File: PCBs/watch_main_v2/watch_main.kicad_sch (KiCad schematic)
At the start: 1 part, among them U101 Watch_Outline_V2

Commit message: Schematic v2 complete
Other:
- added sheet STM32 Power (stm32_power.kicad_sch)
- sheet Bluetooth ports: added SWD; removed none
- sheet Display Connector ports: added AVDD, ELVDD, ELVSS, SWIRE, TP_I2C, TP_INT, TP_RST; removed +4V6, -2V2, OLED_EN
- sheet Display Power ports: added AVDD, AVDDEN, ELVDD, ELVSS, SWIRE; removed none
- sheet Expansion Connector ports: added GPIO1, GPIO2, NRF_SWD, STM32_SWD, UART, USB; removed none
- sheet STM32 ports: added AVDDEN, GPIO1, GPIO2, I2C2, I2C6, SPI1, SWD, SWIRE, TP_INT, TP_RST, USART1, USART6, USB; removed USART2
- sheet Sensors ports: added SPI; removed none
- note added: "Power"
- note removed: "RF Circuits"
- moved on the sheet: U101

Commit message: 190 Unrouted traces
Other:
- sheet Bluetooth ports: added none; removed SWD
- sheet Expansion Connector ports: added none; removed NRF_SWD, STM32_SWD
- sheet Micro SD ports: added EN; removed none
- sheet STM32 ports: added none; removed SWD
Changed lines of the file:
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@@
+    (stroke (width 0) (type default))
+  )
+  (wire (pts (xy 165.1 76.2) (xy 231.14 76.2))
     (stroke (width 0) (type default))
   )
@@
     (stroke (width 0) (type default))
   )
-  (bus (pts (xy 165.1 88.9) (xy 231.14 88.9))
+  (bus (pts (xy 165.1 91.44) (xy 231.14 91.44))
     (stroke (width 0) (type default))
   )
@@
     (stroke (width 0) (type default))
   )
-  (bus (pts (xy 63.5 81.28) (xy 73.66 81.28))
-    (stroke (width 0) (type default))
-  )
   (wire (pts (xy 165.1 33.02) (xy 185.42 33.02))
     (stroke (width 0) (type default))
@@
     (stroke (width 0) (type default))
   )
-  (bus (pts (xy 63.5 78.74) (xy 129.54 78.74))
-    (stroke (width 0) (type default))
-  )
   (wire (pts (xy 63.5 25.4) (xy 129.54 25.4))
     (stroke (width 0) (type default))
@@
     (stroke (width 0) (type default))
   )
-  (bus (pts (xy 73.66 88.9) (xy 73.66 81.28))
-    (stroke (width 0) (type default))
-  )
   (bus (pts (xy 88.9 134.62) (xy 88.9 147.32))
     (stroke (width 0) (type default))
@@
     (stroke (width 0) (type default))
   )
-  (wire (pts (xy 165.1 91.44) (xy 231.14 91.44))
+  (wire (pts (xy 165.1 93.98) (xy 231.14 93.98))
     (stroke (width 0) (type default))
   )
@@
     (stroke (width 0) (type default))
   )
-  (wire (pts (xy 165.1 93.98) (xy 231.14 93.98))
+  (wire (pts (xy 165.1 96.52) (xy 231.14 96.52))
     (stroke (width 0) (type default))
   )
@@
   )
   (wire (pts (xy 63.5 129.54) (xy 83.82 129.54))
-    (stroke (width 0) (type default))
-  )
-  (bus (pts (xy 83.82 88.9) (xy 73.66 88.9))
     (stroke (width 0) (type default))
   )
@@
     (effects (font (size 1.27 1.27)) (justify left bottom))
   )
-  (label "STM32_SWD{SWD}" (at 88.9 78.74 0) (fields_autoplaced)
-    (effects (font (size 1.27 1.27)) (justify left bottom))
-  )
   (label "SPI1{SPI}" (at 170.18 109.22 0) (fields_autoplaced)
     (effects (font (size 1.27 1.27)) (justify left bottom))
   )
-  (label "NRF_SWD{SWD}" (at 66.04 81.28 0) (fields_autoplaced)
-    (effects (font (size 1.27 1.27)) (justify left bottom))
-  )
   (label "LPUART1{UART}" (at 111.76 88.9 0) (fields_autoplaced)
     (effects (font (size 1.27 1.27)) (justify left bottom))
@@
     (effects (font (size 1.27 1.27)) (justify left bottom))
   )
-  (label "I2C1{I2C}" (at 193.04 88.9 0) (fields_autoplaced)
+  (label "I2C1{I2C}" (at 193.04 91.44 0) (fields_autoplaced)
     (effects (font (size 1.27 1.27)) (justify left bottom))
   )
@@
       (effects (font (size 1.27 1.27)) (justify left top))
     )
-    (pin "STM32_SWD" bidirectional (at 63.5 78.74 0)
-      (effects (font (size 1.27 1.27)) (justify right))
-    )
-    (pin "NRF_SWD" bidirectional (at 63.5 81.28 0)
-      (effects (font (size 1.27 1.27)) (justify right))
-    )
     (pin "USB" bidirectional (at 63.5 71.12 0)
       (effects (font (size 1.27 1.27)) (justify right))
@@
     )
   )
-  (sheet (at 231.14 86.36) (size 25.4 10.16) (fields_autoplaced)
+  (sheet (at 231.14 88.9) (size 25.4 10.16) (fields_autoplaced)
     (stroke (width 0.3048) (type solid) (color 108 142 191 1))
     (fill (color 218 232 252 1.0000))
-    (property "Sheetname" "Touch Connector" (at 231.14 85.5722 0)
-      (effects (font (size 1.27 1.27)) (justify left bottom))
-    )
-    (property "Sheetfile" "touch_connector.kicad_sch" (at 231.14 97.1808 0)
-      (effects (font (size 1.27 1.27)) (justify left top))
-    )
-    (pin "I2C" bidirectional (at 231.14 88.9 180)
-      (effects (font (size 1.27 1.27)) (justify left))
-    )
-    (pin "IRQN" output (at 231.14 91.44 180)
-      (effects (font (size 1.27 1.27)) (justify left))
-    )
-    (pin "RST" input (at 231.14 93.98 180)
+    (property "Sheetname" "Touch Connector" (at 231.14 88.1122 0)
+      (effects (font (size 1.27 1.27)) (justify left bottom))
+    )
+    (property "Sheetfile" "touch_connector.kicad_sch" (at 231.14 99.7208 0)
+      (effects (font (size 1.27 1.27)) (justify left top))
+    )
+    (pin "I2C" bidirectional (at 231.14 91.44 180)
+      (effects (font (size 1.27 1.27)) (justify left))
+    )
+    (pin "IRQN" output (at 231.14 93.98 180)
+      (effects (font (size 1.27 1.27)) (justify left))
+    )
+    (pin "RST" input (at 231.14 96.52 180)
       (effects (font (size 1.27 1.27)) (justify left))
     )
@@
       (effects (font (size 1.27 1.27)) (justify right))
     )
-    (pin "SWD" bidirectional (at 83.82 88.9 180)
-      (effects (font (size 1.27 1.27)) (justify left))
-    )
     (instances
       (project "watch_main"
@@
       (effects (font (size 1.27 1.27)) (justify right))
     )
-    (pin "I2C1" bidirectional (at 165.1 88.9 0)
-      (effects (font (size 1.27 1.27)) (justify right))
-    )
-    (pin "TOUCH_RST" output (at 165.1 93.98 0)
-      (effects (font (size 1.27 1.27)) (justify right))
-    )
-    (pin "TOUCH_INT" input (at 165.1 91.44 0)
+    (pin "I2C1" bidirectional (at 165.1 91.44 0)
+      (effects (font (size 1.27 1.27)) (justify right))
+    )
+    (pin "TOUCH_RST" output (at 165.1 96.52 0)
+      (effects (font (size 1.27 1.27)) (justify right))
+    )
+    (pin "TOUCH_INT" input (at 165.1 93.98 0)
       (effects (font (size 1.27 1.27)) (justify right))
     )
@@
     )
     (pin "USB" bidirectional (at 129.54 71.12 180)
-      (effects (font (size 1.27 1.27)) (justify left))
-    )
-    (pin "SWD" bidirectional (at 129.54 78.74 180)
       (effects (font (size 1.27 1.27)) (justify left))
     )
@@
     )
   )
-  (sheet (at 231.14 68.58) (size 25.4 7.62) (fields_autoplaced)
+  (sheet (at 231.14 68.58) (size 25.4 10.16) (fields_autoplaced)
     (stroke (width 0.3048) (type solid) (color 108 142 191 1))
     (fill (color 218 232 252 1.0000))
@@
       (effects (font (size 1.27 1.27)) (justify left bottom))
     )
-    (property "Sheetfile" "micro_sd.kicad_sch" (at 231.14 76.8608 0)
+    (property "Sheetfile" "micro_sd.kicad_sch" (at 231.14 79.4008 0)
       (effects (font (size 1.27 1.27)) (justify left top))
     )
@@
       (effects (font (size 1.27 1.27)) (justify left))
     )
+    (pin "EN" input (at 231.14 76.2 180)
+      (effects (font (size 1.27 1.27)) (justify left))
+    )

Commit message: Main board v2 complete
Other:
- sheet STM32 ports: added SD_EN; removed none

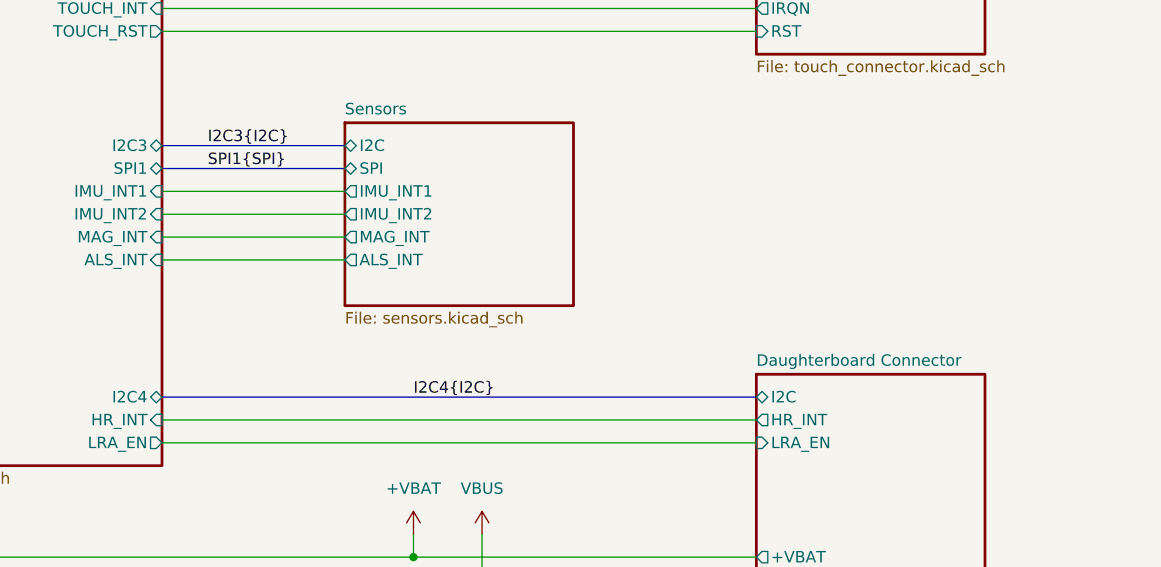
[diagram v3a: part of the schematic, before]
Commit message: Added EEPROM
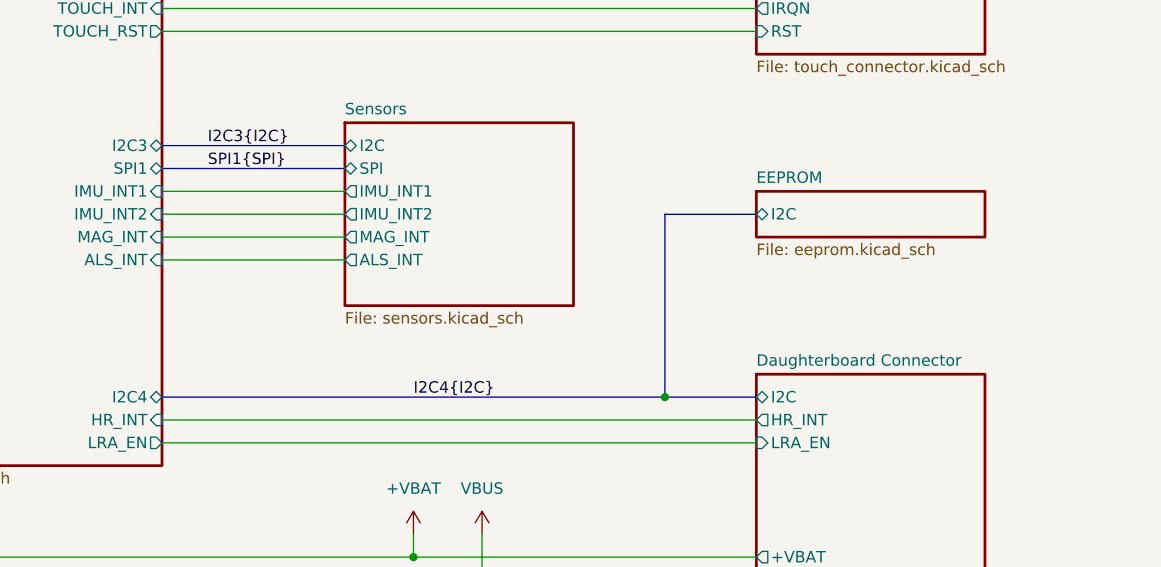
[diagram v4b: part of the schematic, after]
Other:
- added sheet EEPROM (eeprom.kicad_sch)
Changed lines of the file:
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@@
   (junction (at 200.66 154.94) (diameter 0) (color 0 0 0 0)
   )
+  (junction (at 220.98 134.62) (diameter 0) (color 0 0 0 0)
+  )
   (junction (at 73.66 40.64) (diameter 0) (color 0 0 0 0)
   )
@@
     (stroke (width 0) (type default))
   )
+  (bus (pts (xy 220.98 114.3) (xy 220.98 134.62))
+    (stroke (width 0) (type default))
+  )
   (wire (pts (xy 200.66 154.94) (xy 109.22 154.94))
     (stroke (width 0) (type default))
@@
     (stroke (width 0) (type default))
   )
-  (bus (pts (xy 165.1 134.62) (xy 231.14 134.62))
+  (bus (pts (xy 165.1 134.62) (xy 220.98 134.62))
     (stroke (width 0) (type default))
   )
@@
     (stroke (width 0) (type default))
   )
+  (bus (pts (xy 231.14 114.3) (xy 220.98 114.3))
+    (stroke (width 0) (type default))
+  )
   (wire (pts (xy 63.5 76.2) (xy 129.54 76.2))
     (stroke (width 0) (type default))
@@
   )
   (wire (pts (xy 91.44 137.16) (xy 129.54 137.16))
+    (stroke (width 0) (type default))
+  )
+  (bus (pts (xy 220.98 134.62) (xy 231.14 134.62))
     (stroke (width 0) (type default))
   )
@@
       )
     )
+  )
+  (sheet (at 231.14 111.76) (size 25.4 5.08) (fields_autoplaced)
+    (stroke (width 0.3048) (type solid) (color 184 84 80 1))
+    (fill (color 248 206 204 1.0000))
+    (property "Sheetname" "EEPROM" (at 231.14 110.9722 0)
+      (effects (font (size 1.27 1.27)) (justify left bottom))
+    )
+    (property "Sheetfile" "eeprom.kicad_sch" (at 231.14 117.5008 0)
+      (effects (font (size 1.27 1.27)) (justify left top))
+    )
+    (pin "I2C" bidirectional (at 231.14 114.3 180)
+      (effects (font (size 1.27 1.27)) (justify left))
+    )
+    (instances
+      (project "watch_main"
+        (path "/b008648a-c7cf-4e14-8a0a-b9314d757b4a" (page "18"))
+      )
+    )

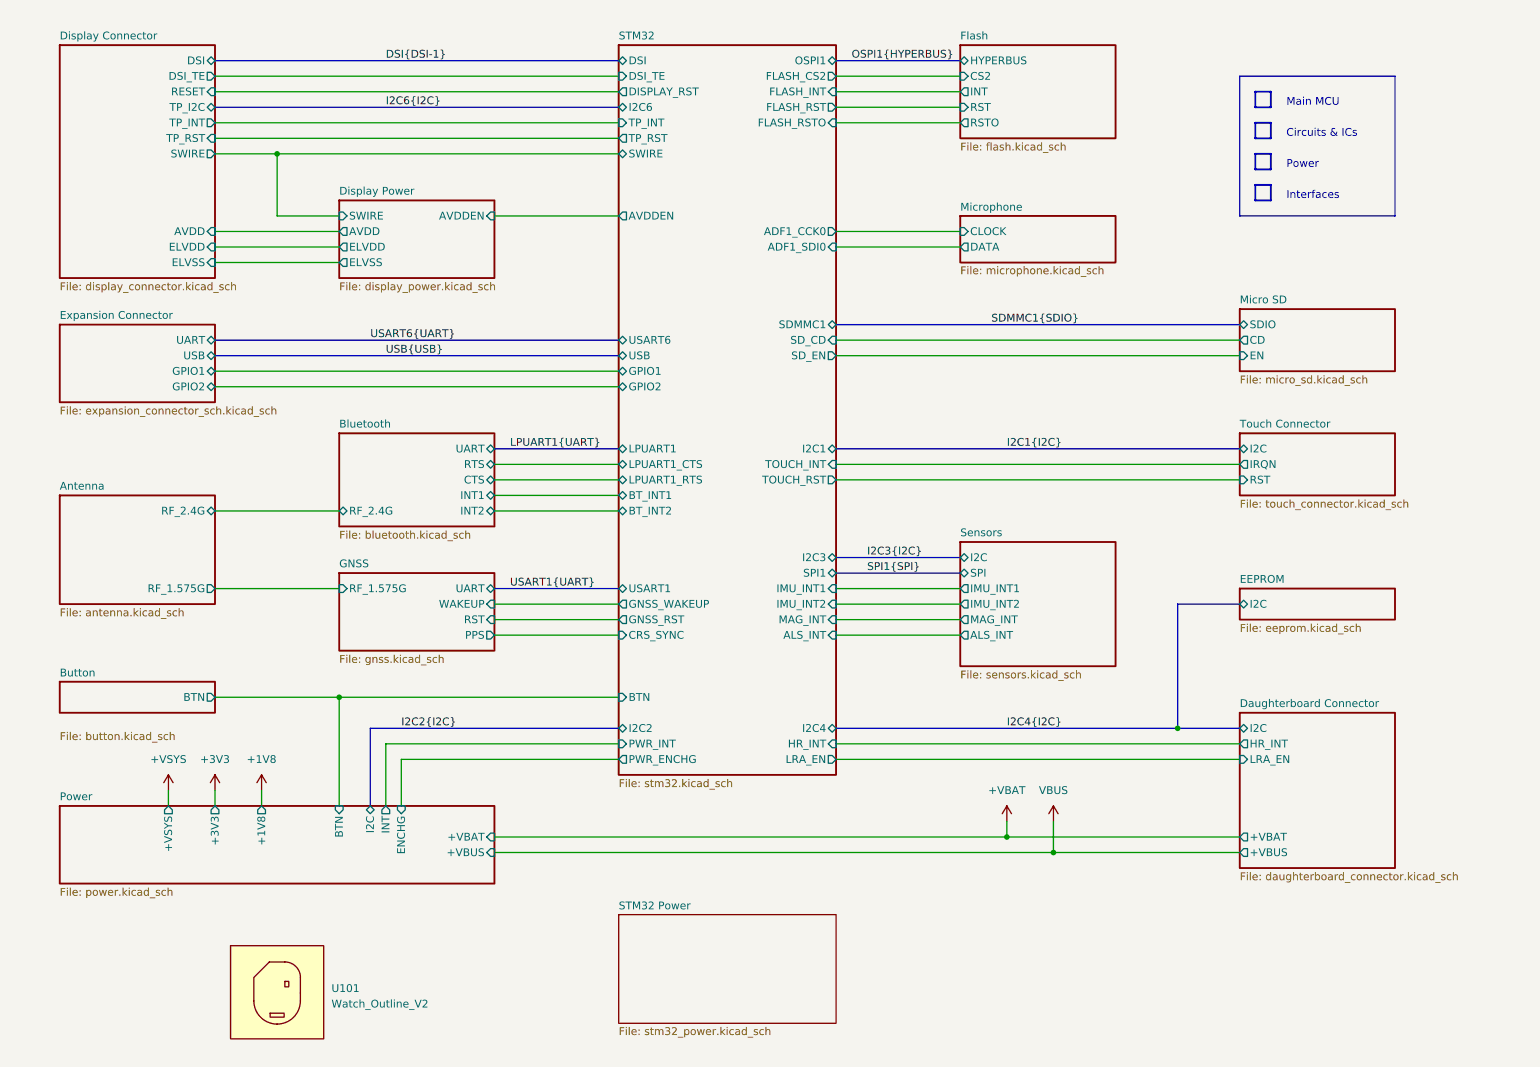
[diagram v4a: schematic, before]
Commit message: Main board and test rig complete & ordered.
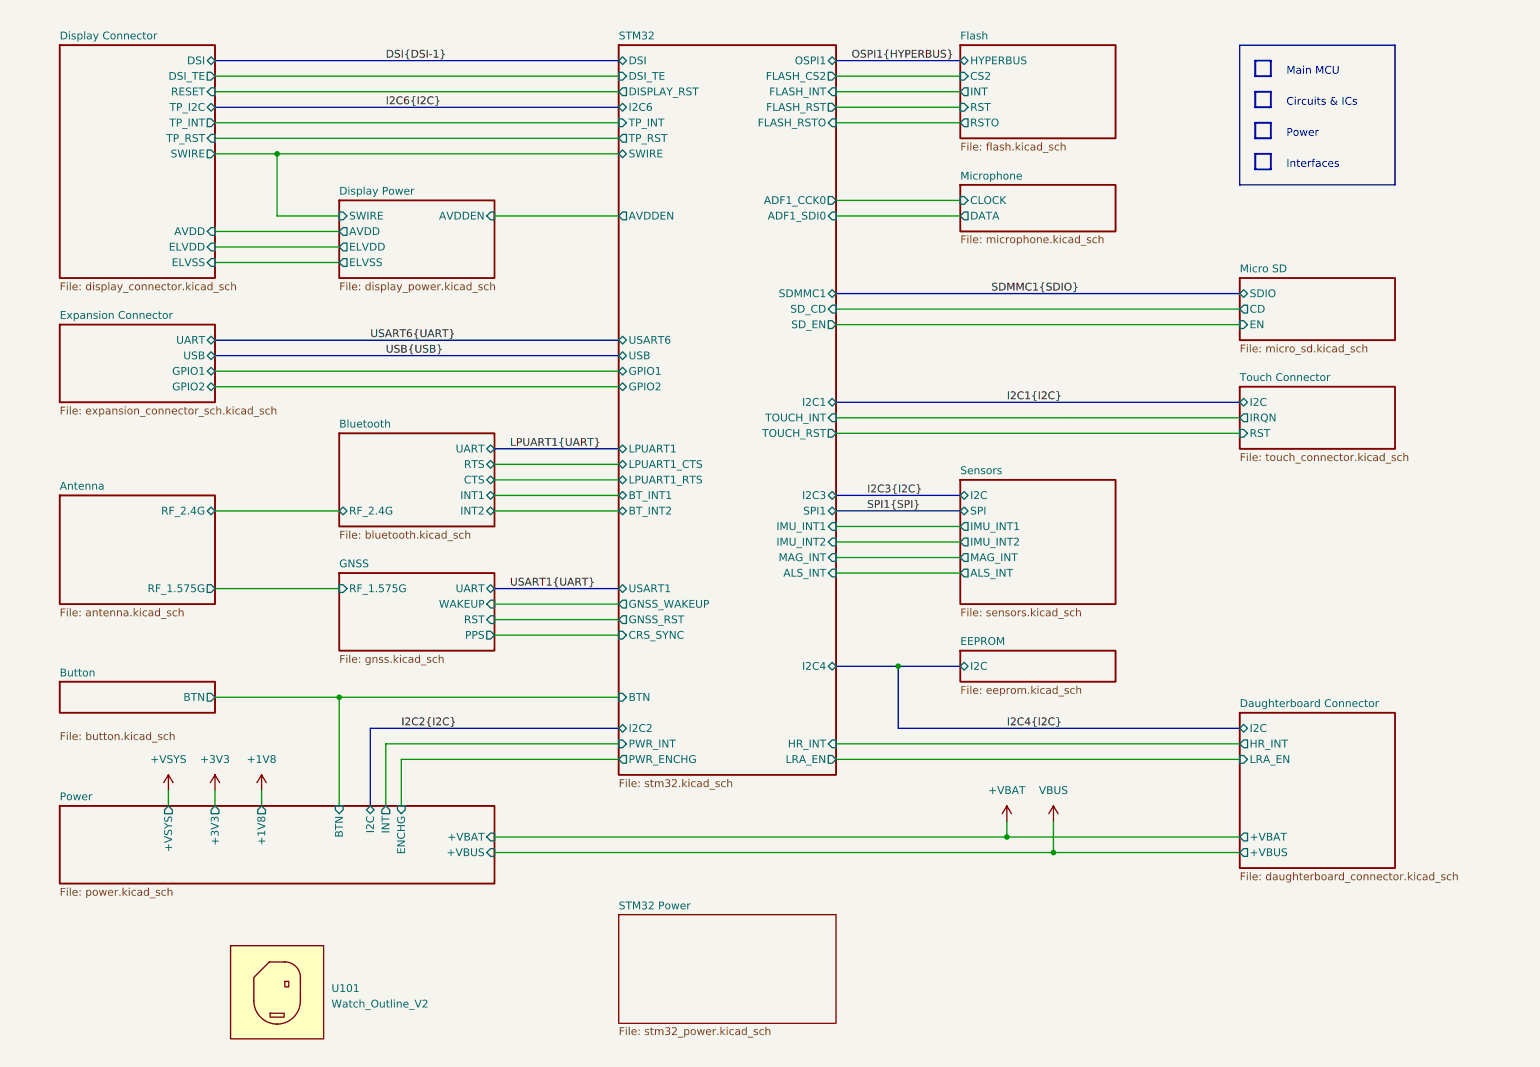
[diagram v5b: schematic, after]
